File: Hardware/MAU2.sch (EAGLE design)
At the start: 11 parts, among them IC1 BMP280, U1 ATTINY85-20SU-SOIC8

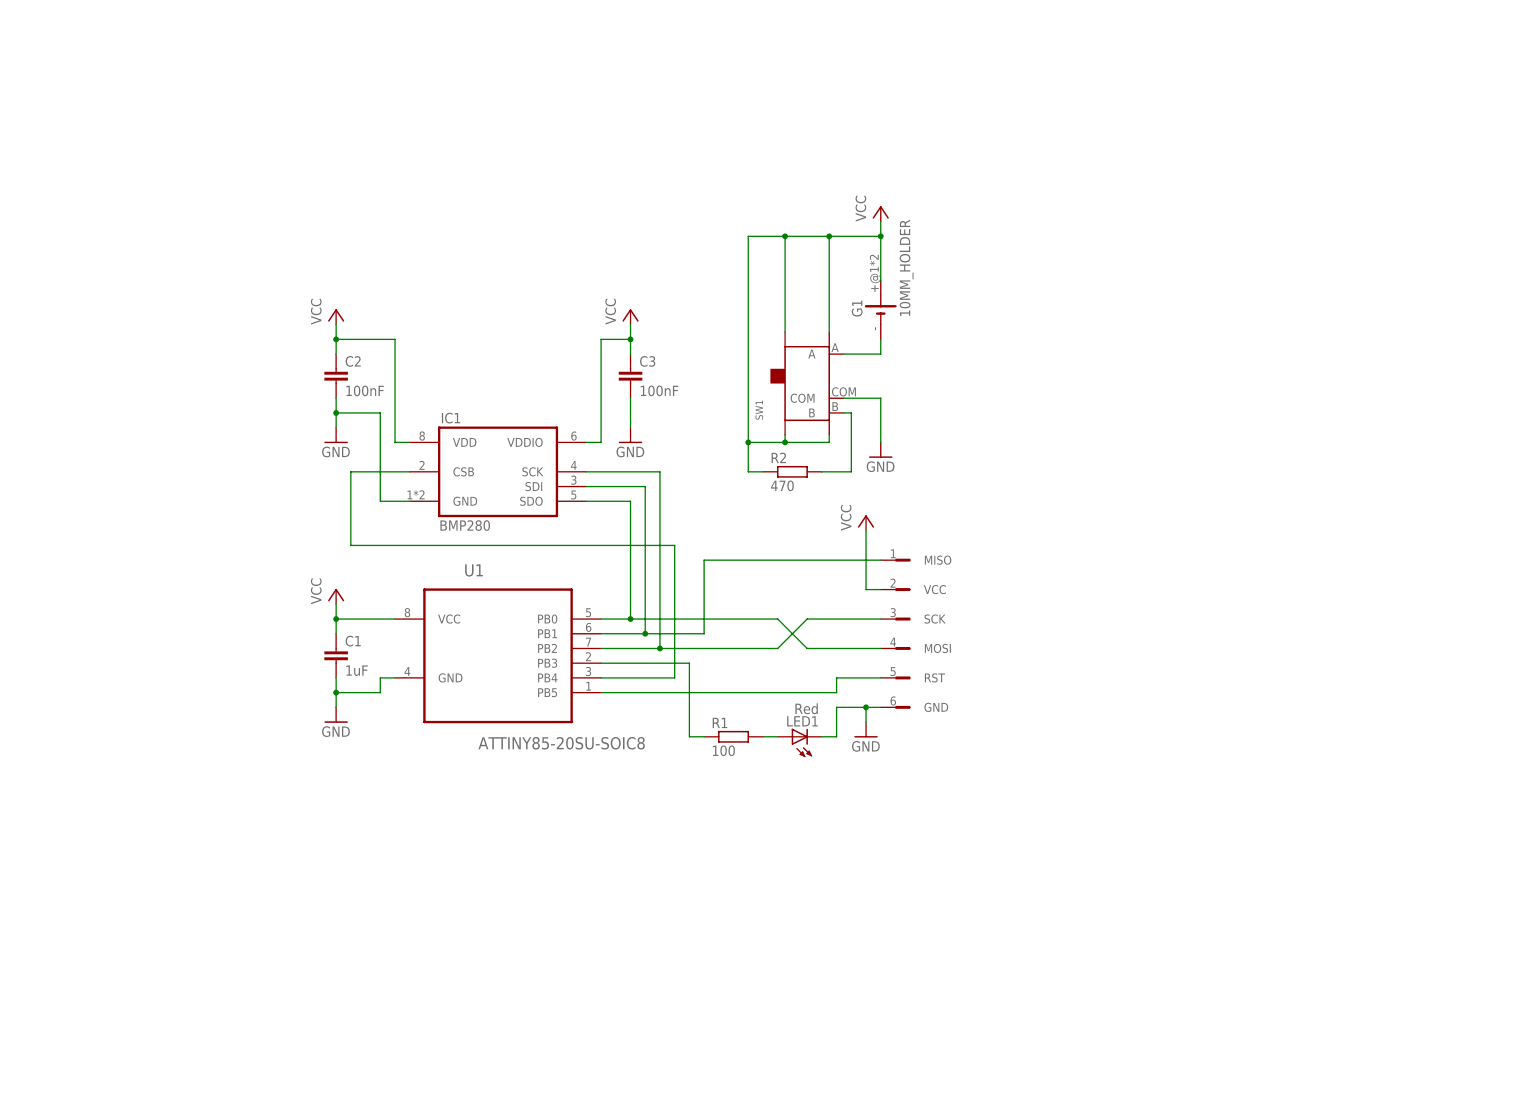
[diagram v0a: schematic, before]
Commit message: MSP430 basic and USB connections (work in progress)
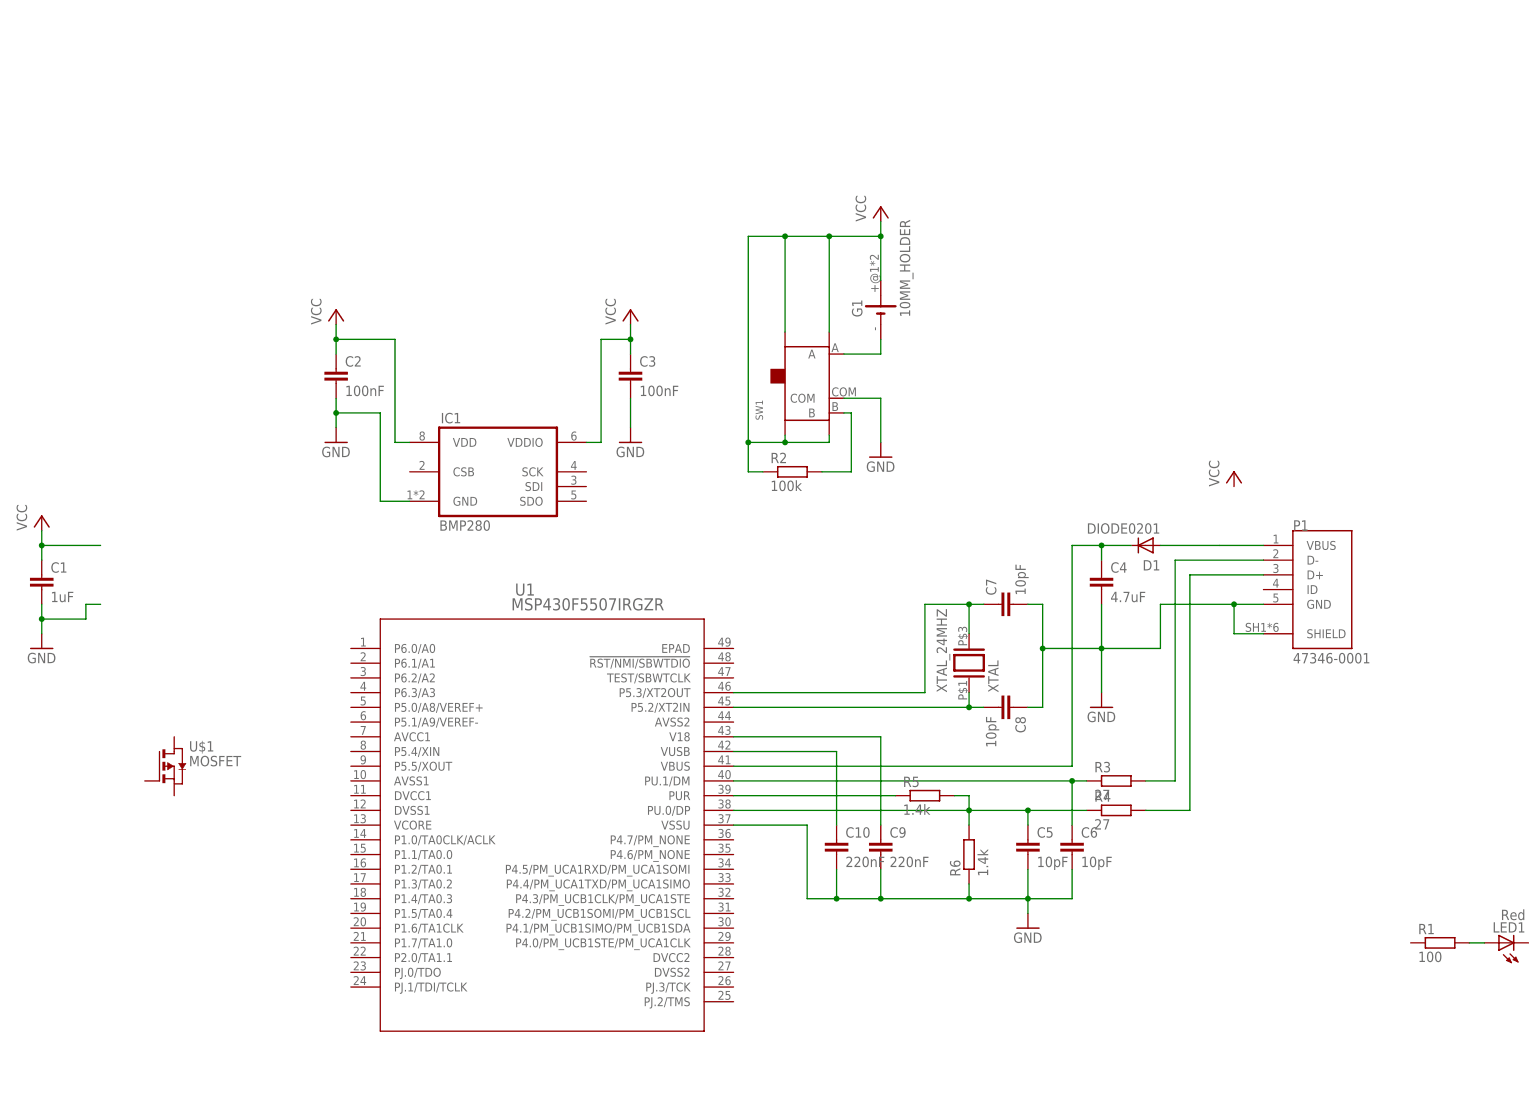
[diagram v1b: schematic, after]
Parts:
- added C10, C9: 220nF, rcl:C-EUC0201
- added C4: 4.7uF, rcl:C-EUC0201
- added C5, C6, C7, C8: 10pF, rcl:C-EUC0201
- added D1: DIODE0201, GenericComponents:DIODE0201
- added P1: 47346-0001, MicroUSB:47346-0001
- added R3, R4: 27, rcl:R-EU_R0201
- added R5, R6: 1.4k, rcl:R-EU_R0201
- added XTAL_24MHZ: XTAL, GenericComponents:XTAL
- R2: value 470 -> 100k
- U$1: value ISP_CONN_6_FDRILL16 -> MOSFET; device altimeter:ISP_CONN_6_FDRILL16 -> GenericComponents:MOSFET
- U1: value ATTINY85-20SU-SOIC8 -> MSP430F5507IRGZR; device Seeed-OPL-ic:MCU-ATTINY85-20SU(SOIC8) -> Texas Instruments MCUs:MSP430F5507IRGZR
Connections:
- new net N$10: R5.1, U1.PUR
- new net N$11: C8.2, U1.P5.2/XT2IN, XTAL_24MHZ.1
- new net N$12: C7.1, U1.P5.3/XT2OUT, XTAL_24MHZ.2
- new net N$13: C9.1, U1.V18
- new net N$14: C10.1, U1.VUSB
- net GND: now also C10.2, C4.2, C5.2, C6.2, C7.2, C8.1, C9.2, P1.GND, P1.SHIELD, R6.1, U1.VSSU; no longer LED1.C, U$1.GND, U1.GND
- net N$2: now also C4.1, D1.C, U1.VBUS; no longer R1.1, U1.PB3
- net N$3: now also D1.A, P1.VBUS; no longer U$1.RST, U1.PB5
- net N$5: now also C6.1, R3.1, U1.PU.1/DM; no longer IC1.CSB, U1.PB4
- net N$7: now also C5.1, R4.1, R5.2, R6.2, U1.PU.0/DP; no longer IC1.SCK, U$1.SCK, U1.PB2
- net N$8: now also P1.D-, R3.2; no longer IC1.SDI, U$1.MISO, U1.PB1
- net N$9: now also P1.D+, R4.2; no longer IC1.SDO, U$1.MOSI, U1.PB0
- net VCC: no longer U$1.VCC, U1.VCC
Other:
- moved on the sheet: C1, LED1, R1

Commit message: Schematics complete
Added connections between MOSFET and DVcc;
Added SPI connections between MSP430 and BMP280;
Added connection between LED and MSP430.
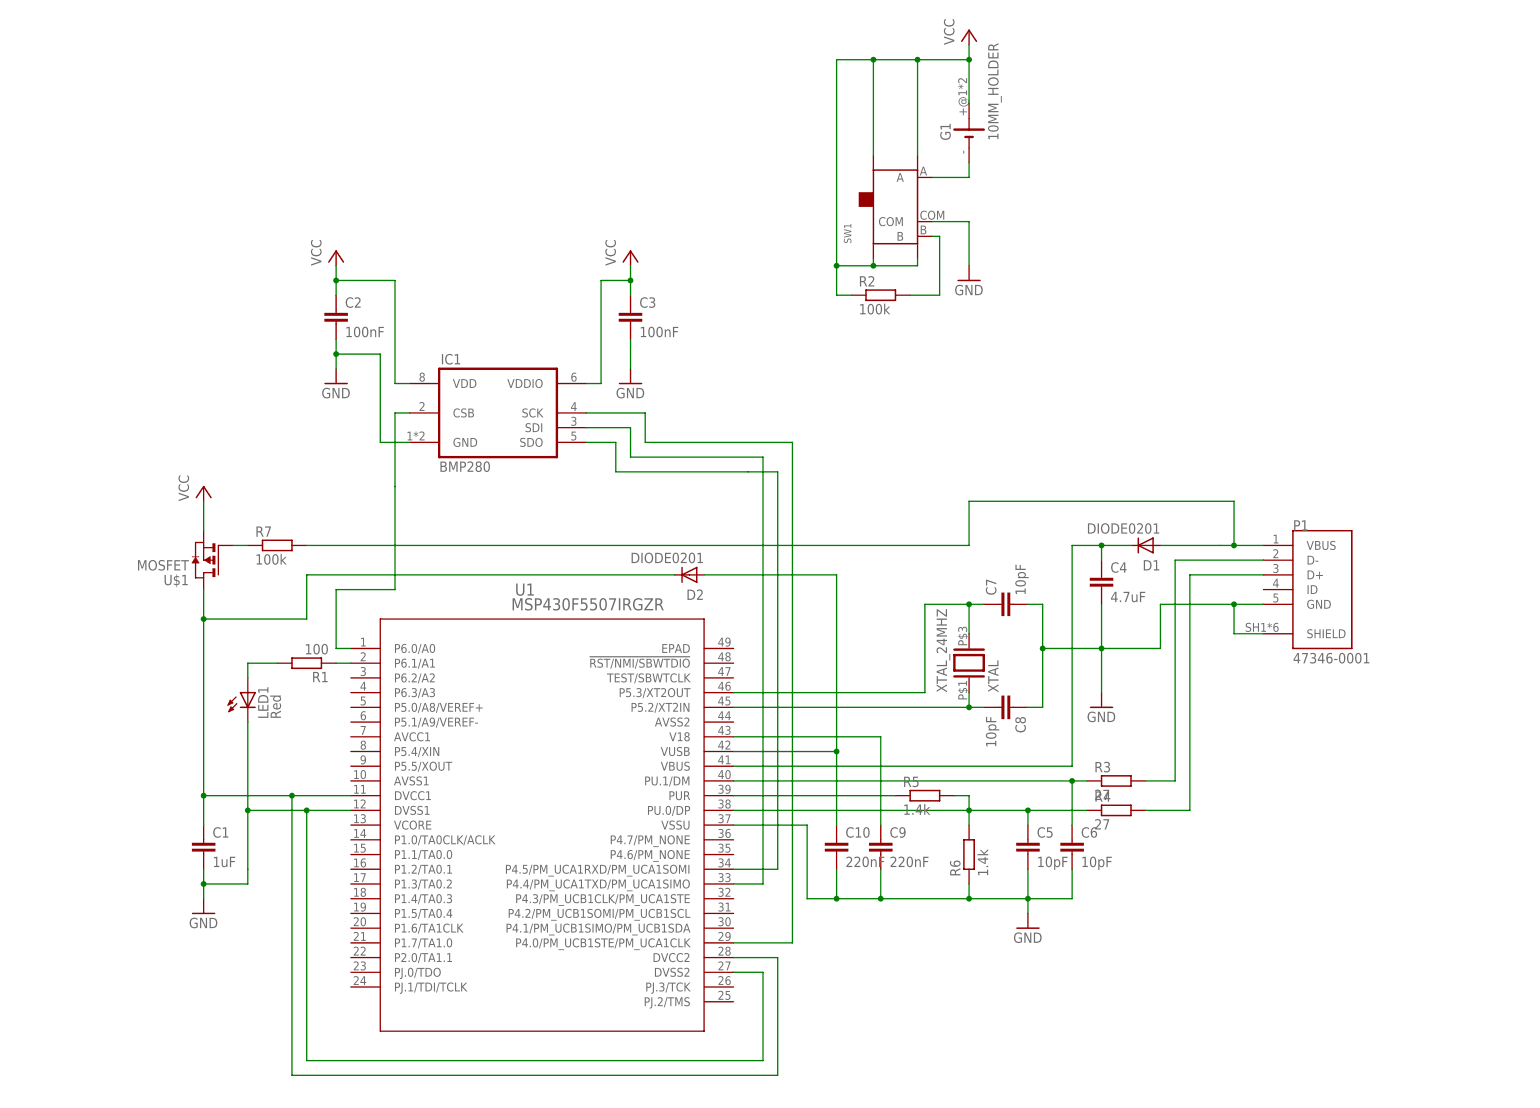
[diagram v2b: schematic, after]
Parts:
- added D2: DIODE0201, GenericComponents:DIODE0201
- added R7: 100k, rcl:R-EU_R0201
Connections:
- new net N$15: R7.1, U$1.G
- new net N$16: IC1.SDO, U1.P4.5/PM_UCA1RXD/PM_UCA1SOMI
- new net N$17: C1.1, D2.C, U$1.D, U1.DVCC1, U1.DVCC2
- new net N$18: IC1.SDI, U1.P4.4/PM_UCA1TXD/PM_UCA1SIMO
- new net N$19: IC1.SCK, U1.P4.0/PM_UCB1STE/PM_UCA1CLK
- new net N$20: IC1.CSB, U1.P6.0/A0
- new net N$21: R1.1, U1.P6.1/A1
- net GND: now also LED1.C, U1.DVSS1, U1.DVSS2
- net N$14: now also D2.A
- net N$3: now also R7.2
- net VCC: now also U$1.S; no longer C1.1
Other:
- moved on the sheet: C1, C2, C3, G1, IC1, LED1, R1, R2, SW1, U$1

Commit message: All CPU needed pins connected and CPU positioned in the board
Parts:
- added C11: 10nF, rcl:C-EUC0201
- C1, C2, C3: device rcl:C-EUC0402 -> rcl:C-EUC0201
- R1, R2: device rcl:R-EU_R0402 -> rcl:R-EU_R0201
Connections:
- new net VCC-FET: C1.1, D2.C, U$1.D, U1.AVCC1, U1.DVCC1, U1.DVCC2
- net GND: now also C11.2, U1.AVSS1, U1.AVSS2, U1.EPAD
- net N$17: now also C11.1, U1.!RST/NMI/SBWTDIO; no longer C1.1, D2.C, U$1.D, U1.DVCC1, U1.DVCC2
- net N$20: now also U1.PJ.2/TMS; no longer U1.P6.0/A0
- net N$21: now also U1.P6.0/A0; no longer U1.P6.1/A1
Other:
- moved on the sheet: C1, LED1, R1, R7, U$1
